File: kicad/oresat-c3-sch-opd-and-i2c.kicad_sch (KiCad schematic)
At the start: 29 parts, among them Q1 NTR2101P, U12 RCLAMP0504FB, U13 MAX892LEUA+T, U24 RV-3028-C7, U30 FM24CL64B-DGTR, U37 LTC4300A-1

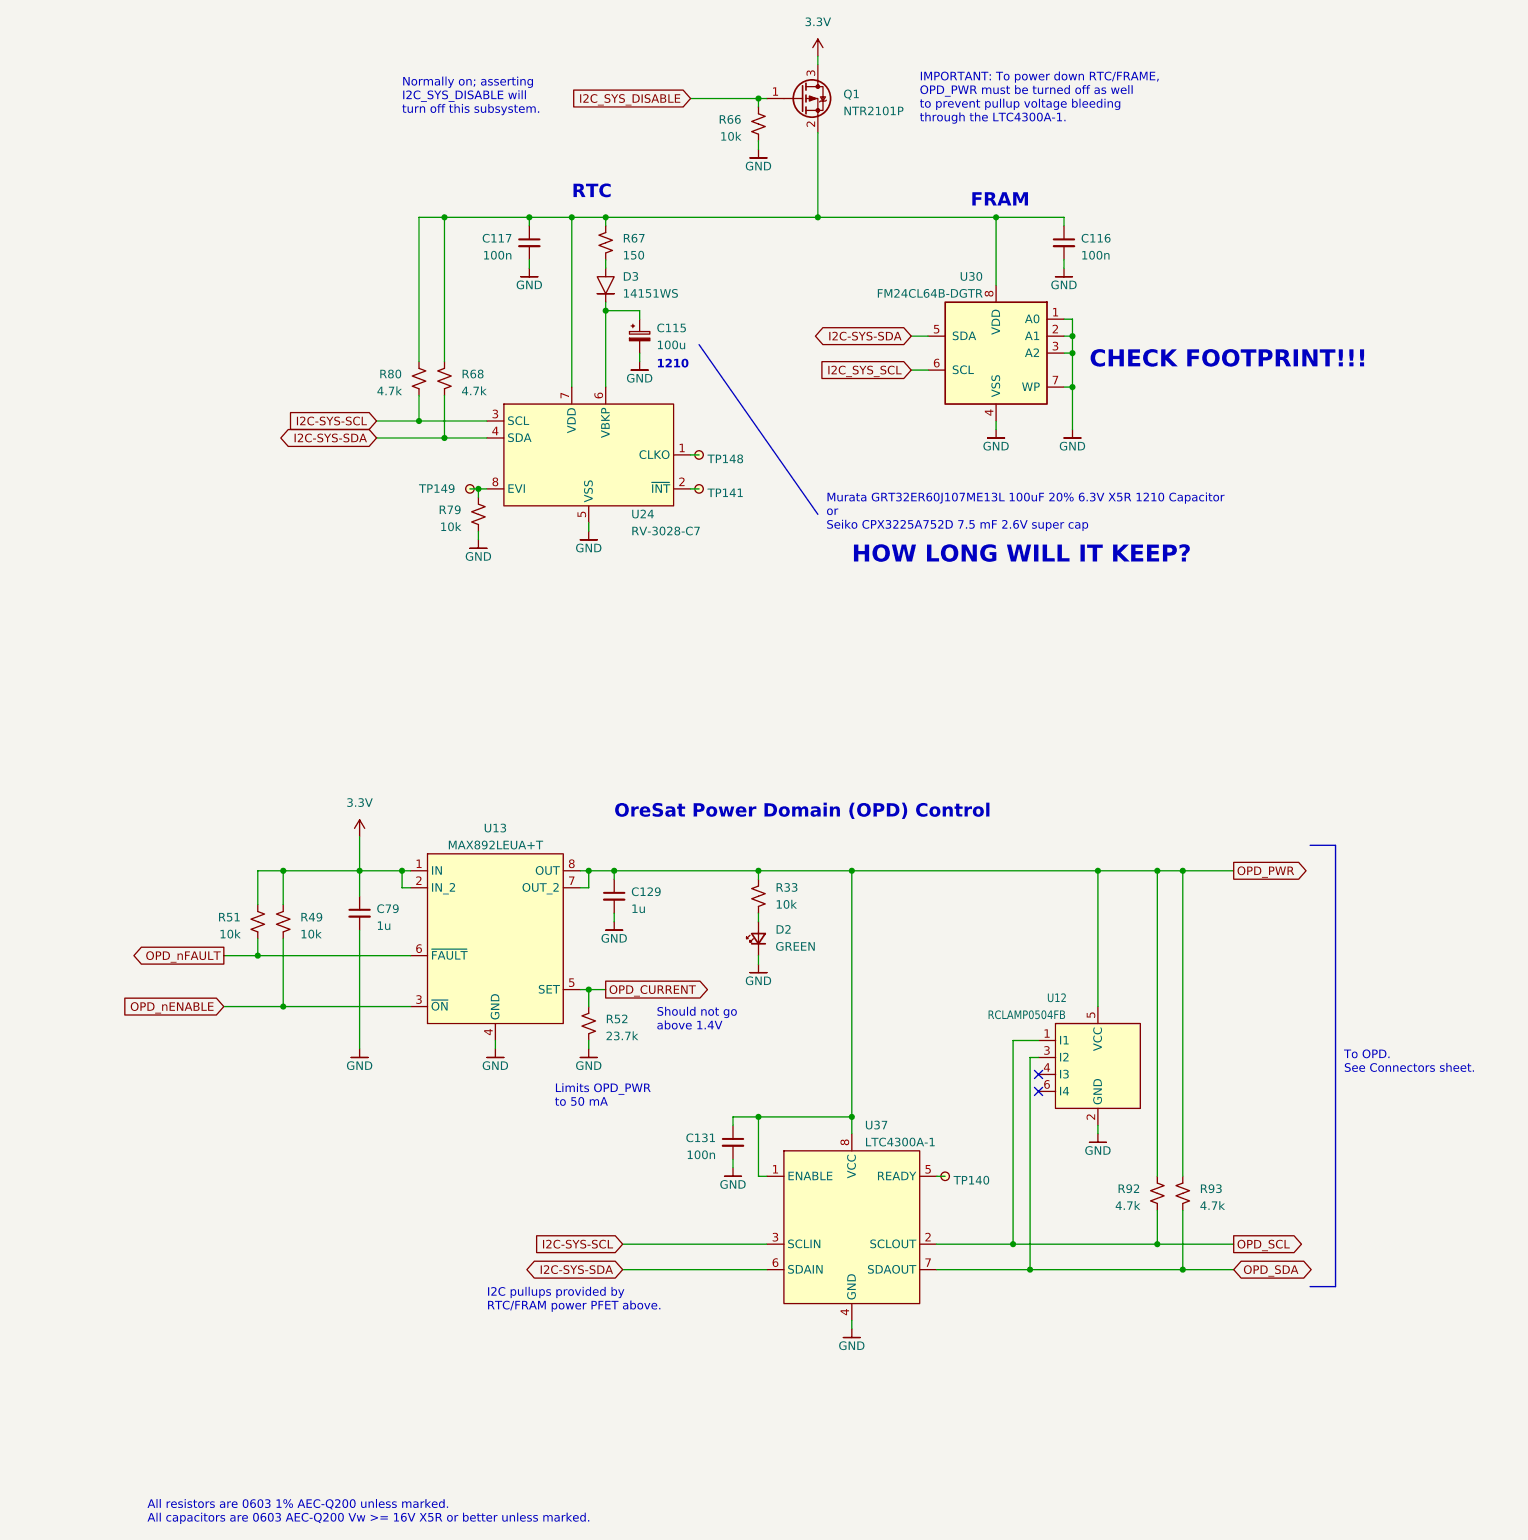
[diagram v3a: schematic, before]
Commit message: Big C3 cleanup with Glenn; radios off of one SPS + separate LDOs, removed lots of test 0 ohm resistors, cleaned up capacitance, and finally wired everything up to the octavo. ZERO ERC errors.
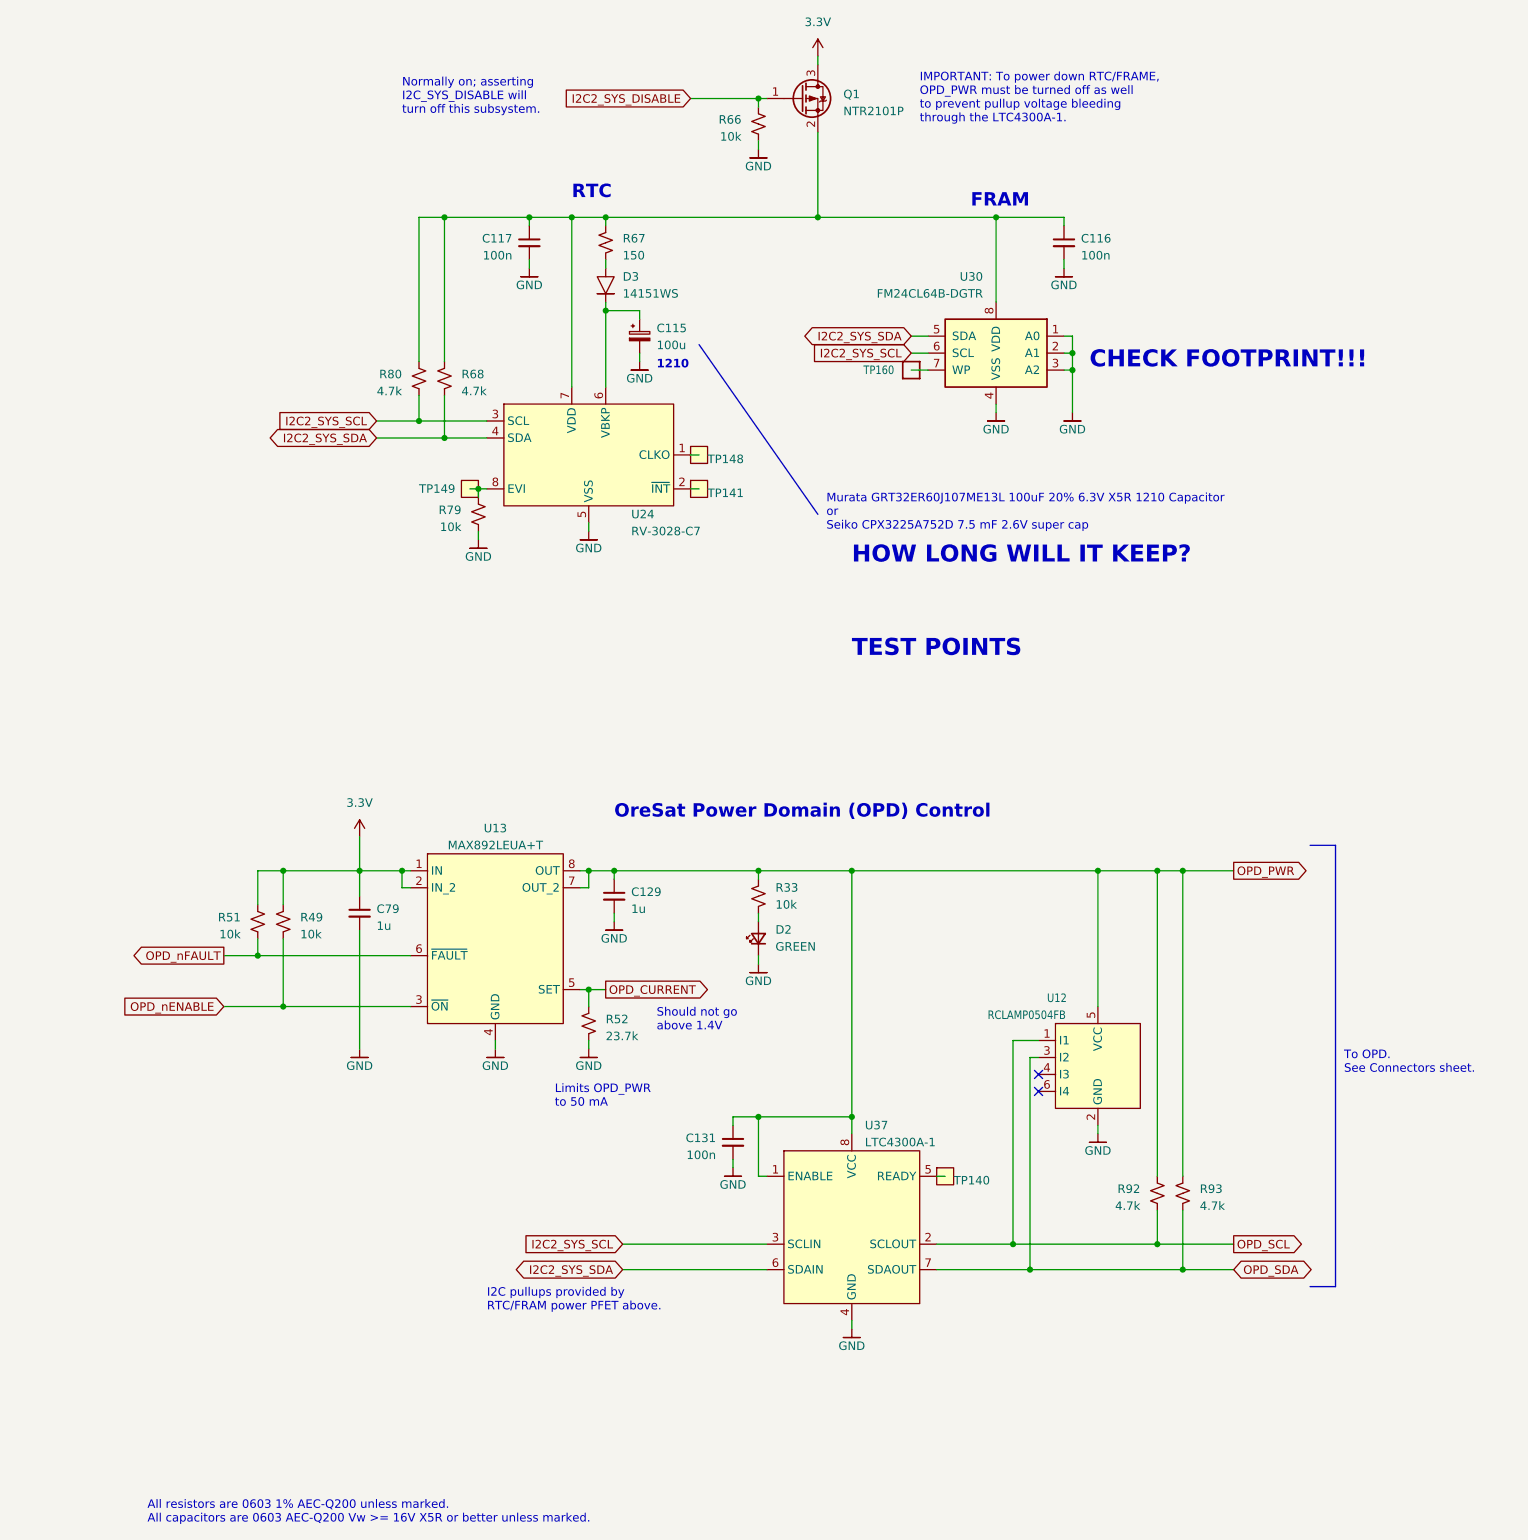
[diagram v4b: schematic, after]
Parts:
- added TP160: Test-Point, TestPoint:TestPoint_Pad_D1.0mm, symbol oresat-misc:Test-Point-1mm-round
- TP140, TP141, TP148, TP149: footprint oresat-misc:TestPoint-MinTH -> TestPoint:TestPoint_Pad_D1.0mm; symbol oresat-misc:TestPoint-MinTH -> oresat-misc:Test-Point-0.75mm-th
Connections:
- net I2C_SYS_SCL is gone; now on net I2C2_SYS_SCL: U30.6 (SCL)
- net GND: no longer U30.7 (WP)
- net I2C-SYS-SCL renamed I2C2_SYS_SCL
- net I2C-SYS-SDA renamed I2C2_SYS_SDA
- net I2C_SYS_DISABLE renamed I2C2_SYS_DISABLE
- new net: TP160.1, U30.7 (WP)
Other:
- note added: "TEST POINTS"

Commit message: Updated test points, fixed some more hidden ERCs.
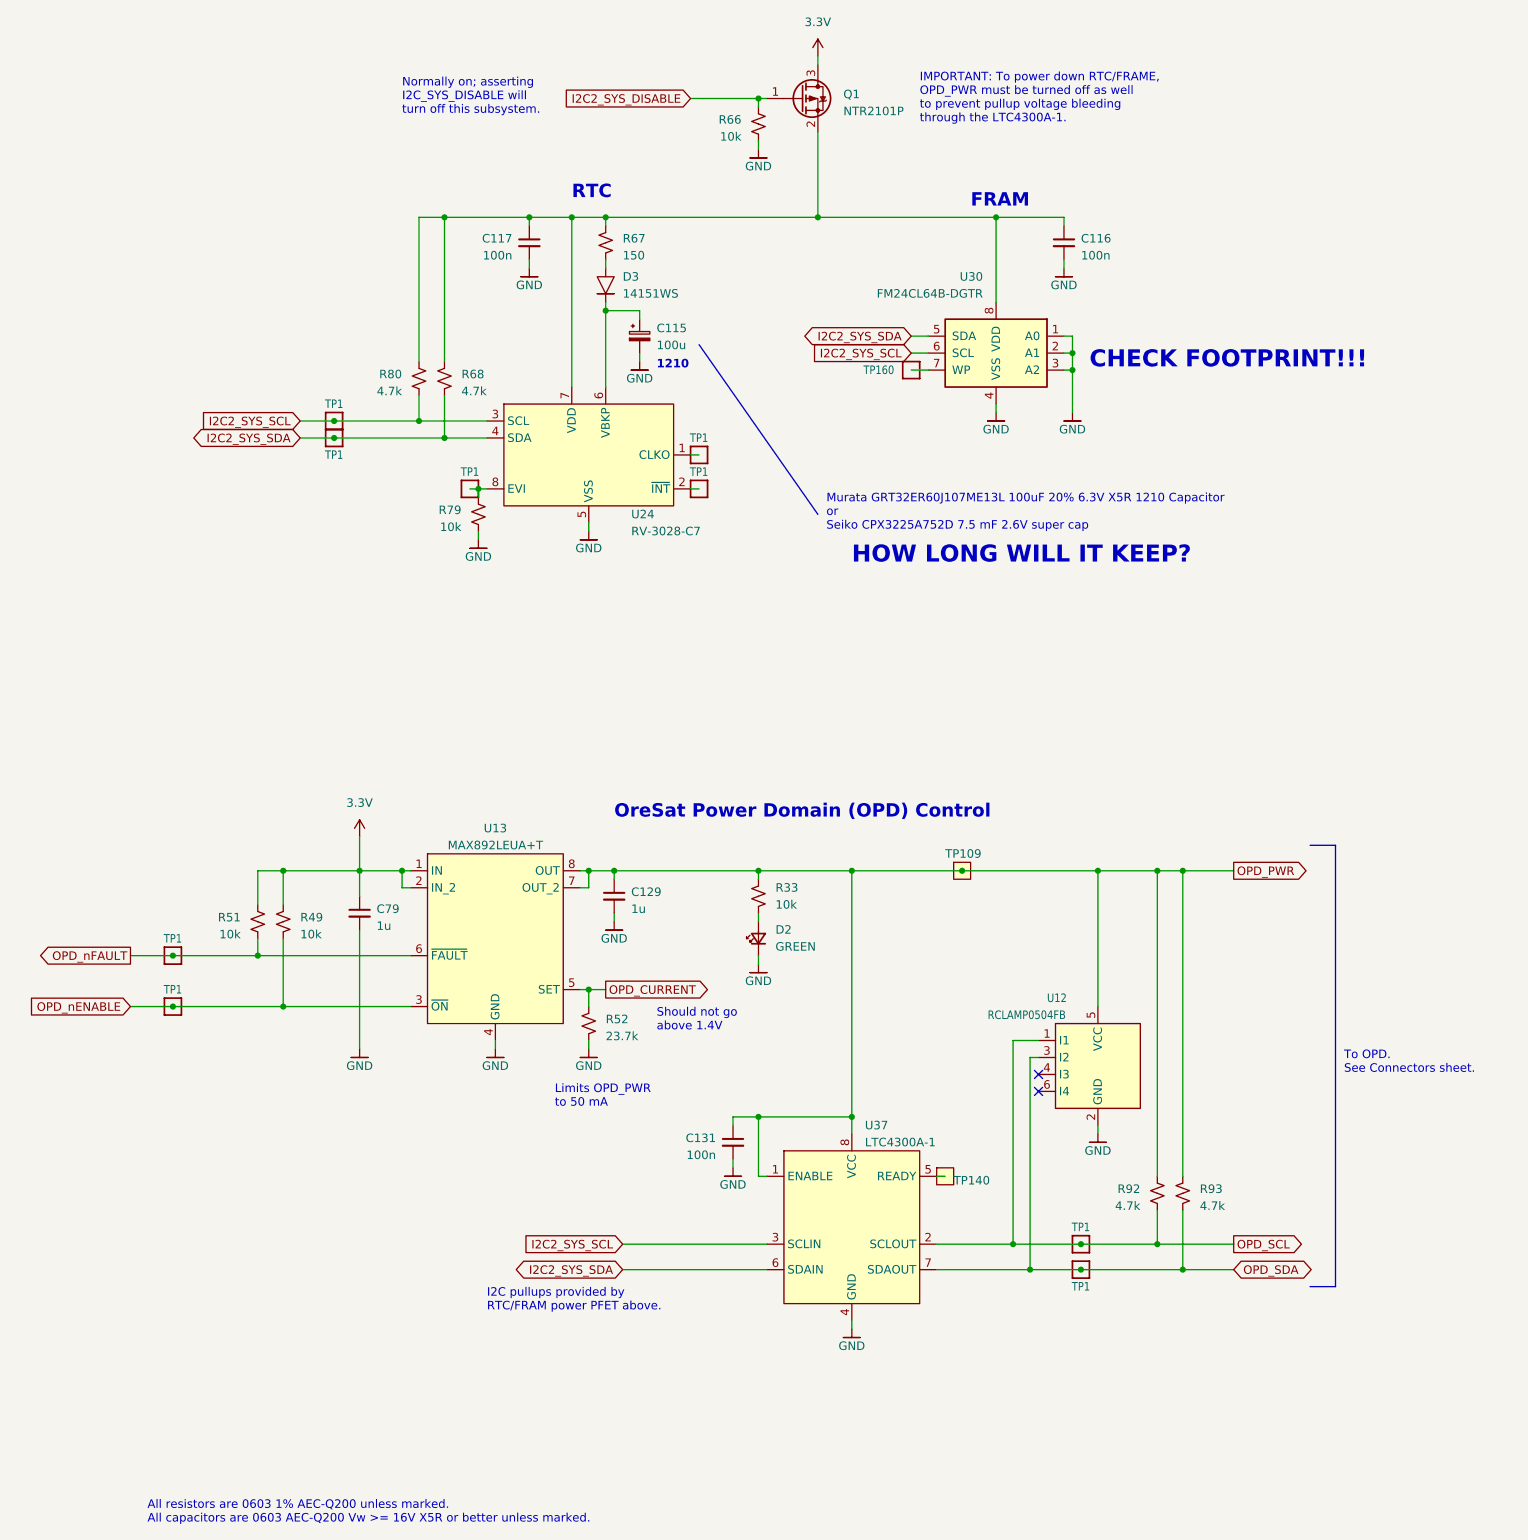
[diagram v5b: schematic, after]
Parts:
- removed TP141, TP148, TP149: TestPoint-MinTH, TestPoint:TestPoint_Pad_D1.0mm, symbol oresat-misc:Test-Point-0.75mm-th
- added TP1 (x9): Test-Point, TestPoint:TestPoint_Pad_D1.0mm, symbol oresat-misc:Test-Point-1mm-round
- added TP109: TestPoint-MinTH, TestPoint:TestPoint_Pad_D1.0mm, symbol oresat-misc:Test-Point-0.75mm-th
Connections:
- net I2C2_SYS_SCL: now also TP1.1
- net I2C2_SYS_SDA: now also TP1.1
- net OPD_PWR: now also TP109.1
- net OPD_SCL: now also TP1.1
- net OPD_SDA: now also TP1.1
- net OPD_nENABLE: now also TP1.1
- net OPD_nFAULT: now also TP1.1
- net at U24.1 (CLKO): now also TP1.1
- net at U24.2 (~{INT}): now also TP1.1
- net at R79.1, U24.8 (EVI): now also TP1.1
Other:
- note removed: "TEST POINTS"

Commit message: Fixed test points; added RF test points. Started on layout and component packages for UHF radio.
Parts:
- TP1, TP160: footprint TestPoint:TestPoint_Pad_D1.0mm -> oresat-misc:TestPoint_Pad_D1.0mm
- TP109, TP140: footprint TestPoint:TestPoint_Pad_D1.0mm -> oresat-misc:TestPoint-0.75mm-th
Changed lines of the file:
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@@
       (effects (font (size 1.27 1.27)) hide)
     )
-    (property "Footprint" "TestPoint:TestPoint_Pad_D1.0mm" (at 143.51 88.9 0)
+    (property "Footprint" "oresat-misc:TestPoint_Pad_D1.0mm" (at 143.51 88.9 0)
       (effects (font (size 1.27 1.27)) hide)
     )
@@
       (effects (font (size 1.27 1.27)) hide)
     )
-    (property "Footprint" "TestPoint:TestPoint_Pad_D1.0mm" (at 237.49 153.67 0)
+    (property "Footprint" "oresat-misc:TestPoint-0.75mm-th" (at 237.49 153.67 0)
       (effects (font (size 1.27 1.27)) hide)
     )
@@
       (effects (font (size 1.27 1.27)) hide)
     )
-    (property "Footprint" "TestPoint:TestPoint_Pad_D1.0mm" (at 219.71 88.9 0)
+    (property "Footprint" "oresat-misc:TestPoint_Pad_D1.0mm" (at 219.71 88.9 0)
       (effects (font (size 1.27 1.27)) hide)
     )
@@
       (effects (font (size 1.27 1.27)) hide)
     )
-    (property "Footprint" "TestPoint:TestPoint_Pad_D1.0mm" (at 198.12 111.76 0)
+    (property "Footprint" "oresat-misc:TestPoint_Pad_D1.0mm" (at 198.12 111.76 0)
       (effects (font (size 1.27 1.27)) hide)
     )
@@
       (effects (font (size 1.27 1.27)) hide)
     )
-    (property "Footprint" "TestPoint:TestPoint_Pad_D1.0mm" (at 255.27 229.87 0)
+    (property "Footprint" "oresat-misc:TestPoint_Pad_D1.0mm" (at 255.27 229.87 0)
       (effects (font (size 1.27 1.27)) hide)
     )
@@
       (effects (font (size 1.27 1.27)) hide)
     )
-    (property "Footprint" "TestPoint:TestPoint_Pad_D1.0mm" (at 143.51 106.68 0)
+    (property "Footprint" "oresat-misc:TestPoint_Pad_D1.0mm" (at 143.51 106.68 0)
       (effects (font (size 1.27 1.27)) hide)
     )
@@
       (effects (font (size 1.27 1.27)) hide)
     )
-    (property "Footprint" "TestPoint:TestPoint_Pad_D1.0mm" (at 119.38 194.31 0)
+    (property "Footprint" "oresat-misc:TestPoint_Pad_D1.0mm" (at 119.38 194.31 0)
       (effects (font (size 1.27 1.27)) hide)
     )
@@
       (effects (font (size 1.27 1.27)) hide)
     )
-    (property "Footprint" "TestPoint:TestPoint_Pad_D1.0mm" (at 163.83 116.84 0)
+    (property "Footprint" "oresat-misc:TestPoint_Pad_D1.0mm" (at 163.83 116.84 0)
       (effects (font (size 1.27 1.27)) hide)
     )
@@
       (effects (font (size 1.27 1.27)) hide)
     )
-    (property "Footprint" "TestPoint:TestPoint_Pad_D1.0mm" (at 234.95 199.39 0)
+    (property "Footprint" "oresat-misc:TestPoint-0.75mm-th" (at 234.95 199.39 0)
       (effects (font (size 1.27 1.27)) hide)
     )
@@
       (effects (font (size 1.27 1.27)) hide)
     )
-    (property "Footprint" "TestPoint:TestPoint_Pad_D1.0mm" (at 198.12 116.84 0)
+    (property "Footprint" "oresat-misc:TestPoint_Pad_D1.0mm" (at 198.12 116.84 0)
       (effects (font (size 1.27 1.27)) hide)
     )
@@
       (effects (font (size 1.27 1.27)) hide)
     )
-    (property "Footprint" "TestPoint:TestPoint_Pad_D1.0mm" (at 255.27 213.36 0)
+    (property "Footprint" "oresat-misc:TestPoint_Pad_D1.0mm" (at 255.27 213.36 0)
       (effects (font (size 1.27 1.27)) hide)
     )
@@
       (effects (font (size 1.27 1.27)) hide)
     )
-    (property "Footprint" "TestPoint:TestPoint_Pad_D1.0mm" (at 119.38 186.69 0)
-      (effects (font (size 1.27 1.27)) hide)
-    )
+    (property "Footprint" "oresat-misc:TestPoint_Pad_D1.0mm" (at 119.38 186.69 0)
+      (effects (font (size 1.27 1.27)) hide)
+    )
